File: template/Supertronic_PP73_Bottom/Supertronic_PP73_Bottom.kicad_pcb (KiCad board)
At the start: 2 copper layers, 58 x 58 mm, 5 parts

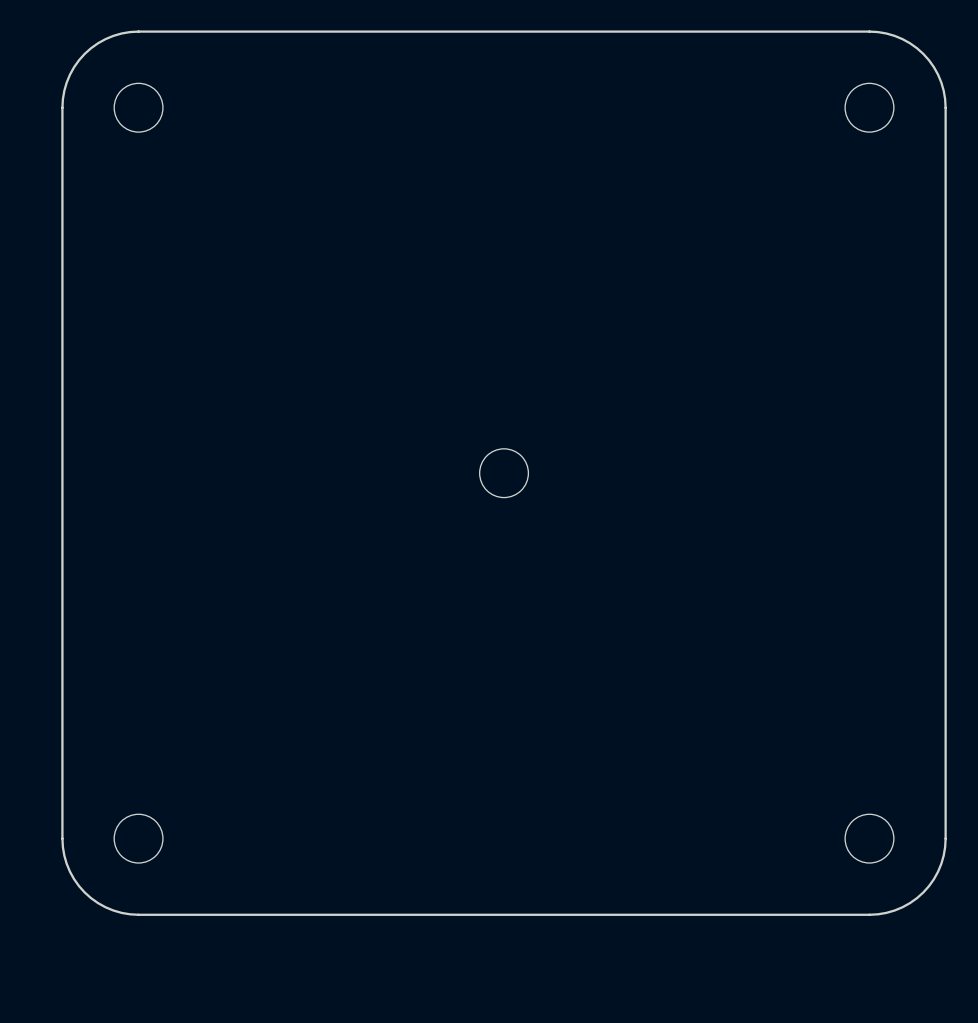
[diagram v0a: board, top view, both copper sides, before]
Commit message: Updated templates
Added mounting holes on schematics, dimensions and re-adjusted board
sizes
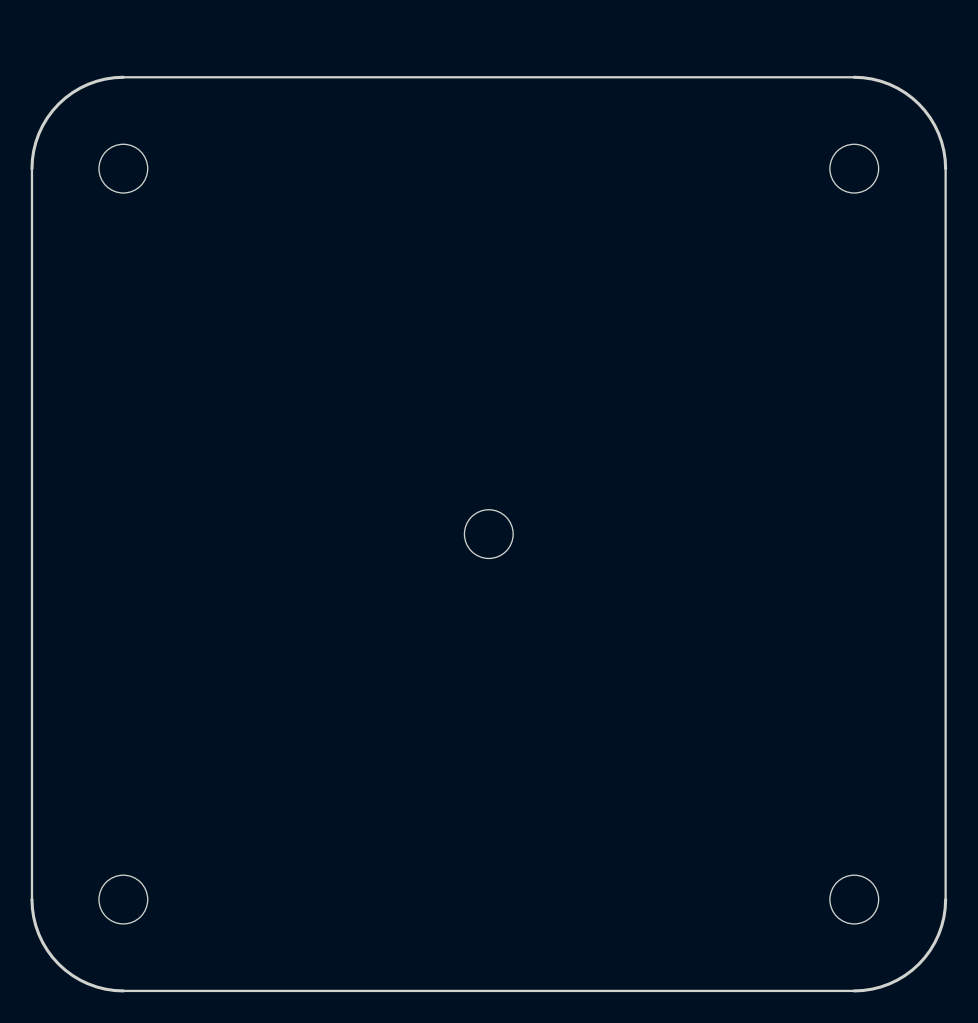
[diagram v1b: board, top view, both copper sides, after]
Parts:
- H1, H2, H3, H4, H5: renamed from REF**; value MountingHole_3.2mm_M3 -> MountingHole
- moved H1 4.12 mm to (121.0, 76.0)
- moved H2 4.12 mm to (169.0, 76.0)
- moved H3 4.12 mm to (169.0, 124.0)
- moved H4 4.12 mm to (121.0, 124.0)
- moved H5 4.12 mm to (145.0, 100.0)
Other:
- board size 58 x 58 mm -> 60 x 60 mm
